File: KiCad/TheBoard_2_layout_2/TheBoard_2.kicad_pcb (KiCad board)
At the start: 2 copper layers, 150 x 100 mm, 165 parts, among them J1 Conn_01x03_Female, J2 Conn_01x03_Female, J3 Conn_01x16_Female, J4 DB37_Male_MountingHoles, J5 Conn_01x16_Female, J6 Conn_01x02_Male, J7 Conn_01x02_Pin, J8 Conn_01x02_Male, U1 MAX680CSA+T, U10 MCP6074-E/SL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

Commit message: power connection
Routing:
- net +2V5: track 300.7 -> 409.1 mm, vias 16 -> 17
- net +5V: track 412.5 -> 486.2 mm
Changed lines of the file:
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@@
   (segment (start 127.75 133.5) (end 136.75 133.5) (width 1.6) (layer "F.Cu") (net 1))
   (segment (start 146.75 121.75) (end 147 121.5) (width 1.6) (layer "F.Cu") (net 1))
+  (segment (start 144.75 141.5) (end 207.17 141.5) (width 1.6) (layer "F.Cu") (net 1))
+  (segment (start 136.75 133.5) (end 144.75 141.5) (width 1.6) (layer "F.Cu") (net 1))
   (via (at 108.30572 72.859279) (size 0.8) (drill 0.4) (layers "F.Cu" "B.Cu") (net 1))
   (via (at 200.5 103) (size 0.8) (drill 0.4) (layers "F.Cu" "B.Cu") (net 1))
@@
   (segment (start 108.30572 77.109279) (end 107.46822 77.109279) (width 0.6) (layer "F.Cu") (net 2))
   (segment (start 107.501779 118.366203) (end 108.201203 118.366203) (width 0.6) (layer "F.Cu") (net 2))
+  (segment (start 127.75 144.5) (end 208.75 144.5) (width 1.6) (layer "F.Cu") (net 2))
   (segment (start 200.5 98.5) (end 199.6625 98.5) (width 0.6) (layer "F.Cu") (net 2))
   (segment (start 199.6625 112.5) (end 200.5 112.5) (width 0.6) (layer "F.Cu") (net 2))
   (segment (start 108.4 99.775) (end 109.1925 99.775) (width 0.6) (layer "F.Cu") (net 2))
   (segment (start 108.375 113.75) (end 109.1675 113.75) (width 0.6) (layer "F.Cu") (net 2))
+  (segment (start 209.71 143.46) (end 209.71 141.5) (width 1.6) (layer "F.Cu") (net 2))
   (segment (start 200.5 76.75) (end 201.3375 76.75) (width 0.6) (layer "F.Cu") (net 2))
   (segment (start 108.201203 118.366203) (end 109.176779 118.366203) (width 0.6) (layer "F.Cu") (net 2))
@@
   (segment (start 199.524032 130.700961) (end 200.361532 130.700961) (width 0.6) (layer "F.Cu") (net 2))
   (segment (start 200.5 63) (end 201.3375 63) (width 0.6) (layer "F.Cu") (net 2))
+  (segment (start 209.75 143.5) (end 209.71 143.46) (width 1.6) (layer "F.Cu") (net 2))
+  (segment (start 208.75 144.5) (end 209.75 143.5) (width 1.6) (layer "F.Cu") (net 2))
   (segment (start 109.14322 63.109279) (end 108.30572 63.109279) (width 0.6) (layer "F.Cu") (net 2))
   (segment (start 199.6625 76.75) (end 200.5 76.75) (width 0.6) (layer "F.Cu") (net 2))
@@
   (segment (start 108.701203 132.616203) (end 109.426779 132.616203) (width 0.6) (layer "F.Cu") (net 2))
   (via (at 108.201203 118.366203) (size 0.8) (drill 0.4) (layers "F.Cu" "B.Cu") (net 2))
+  (via (at 127.75 144.5) (size 0.8) (drill 0.7) (layers "F.Cu" "B.Cu") (net 2))
   (via (at 108.701203 132.616203) (size 0.8) (drill 0.4) (layers "F.Cu" "B.Cu") (net 2))
   (via (at 200.5 63) (size 0.8) (drill 0.4) (layers "F.Cu" "B.Cu") (net 2))
@@
   (segment (start 200.466487 94.653994) (end 209.556006 94.653994) (width 1.6) (layer "B.Cu") (net 2))
   (segment (start 108.395 77.198559) (end 108.30572 77.109279) (width 1.6) (layer "B.Cu") (net 2))
+  (segment (start 120.585 144.5) (end 127.75 144.5) (width 1.6) (layer "B.Cu") (net 2))
   (segment (start 108.395 99.77) (end 108.4 99.775) (width 1.6) (layer "B.Cu") (net 2))
   (segment (start 99.21 53) (end 99.21 63.25) (width 1.6) (layer "B.Cu") (net 2))
@@
   (segment (start 108.375 118.192406) (end 108.201203 118.366203) (width 1.6) (layer "B.Cu") (net 2))
   (segment (start 209.71 112.5) (end 209.71 94.5) (width 1.6) (layer "B.Cu") (net 2))
+  (segment (start 108.701203 132.616203) (end 120.585 144.5) (width 1.6) (layer "B.Cu") (net 2))
   (segment (start 200.361532 130.700961) (end 209.660961 130.700961) (width 1.6) (layer "B.Cu") (net 2))
   (segment (start 102 132.5) (end 108.585 132.5) (width 1.6) (layer "B.Cu") (net 2))

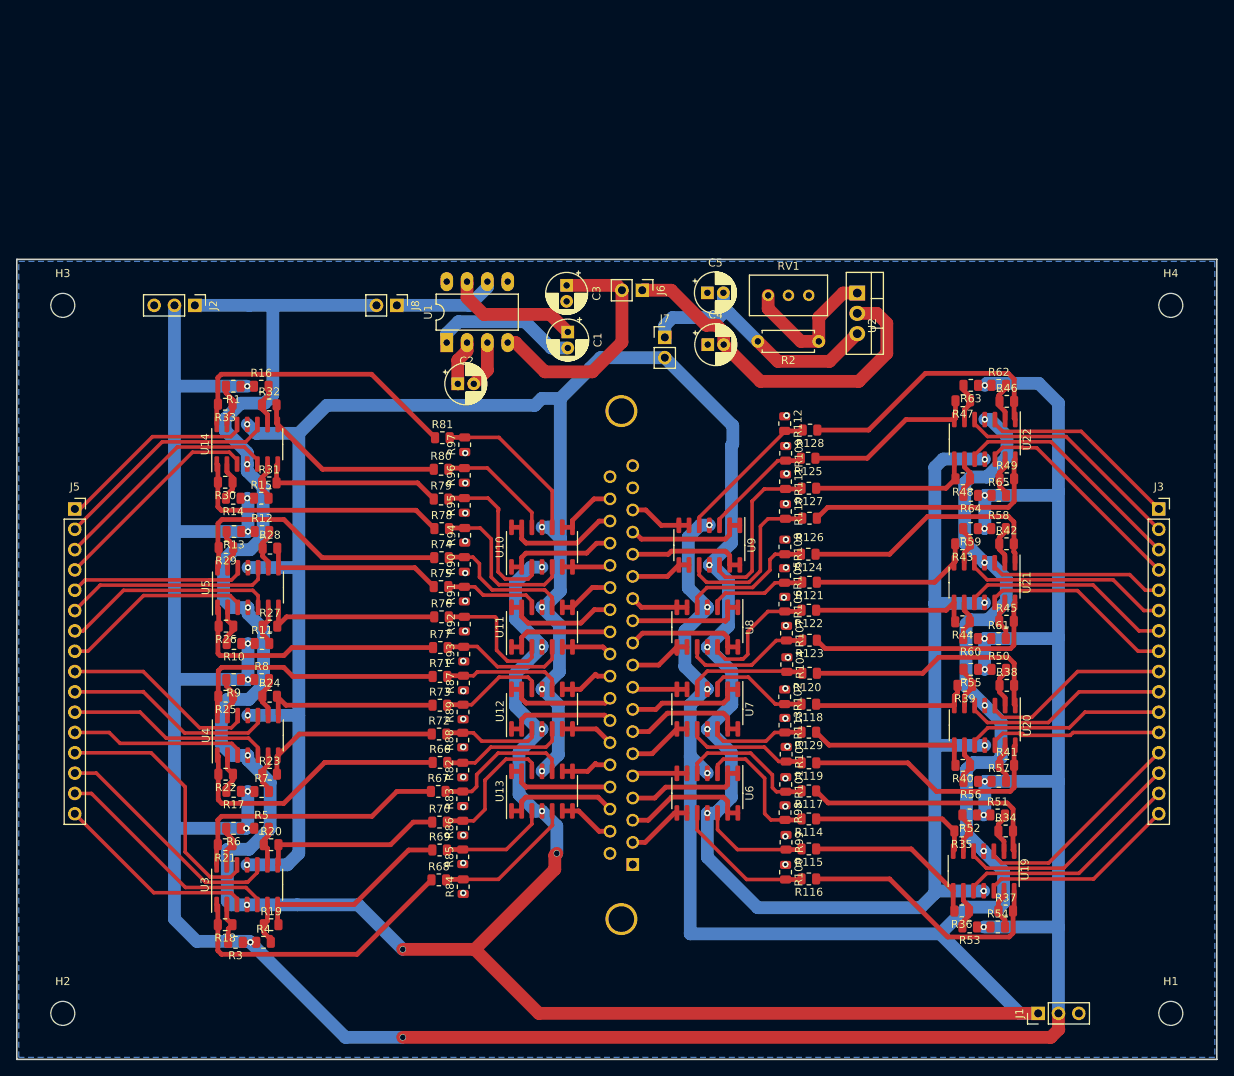
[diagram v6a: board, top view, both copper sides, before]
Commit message: Adding gnd to pot, cleaning vias and tracks
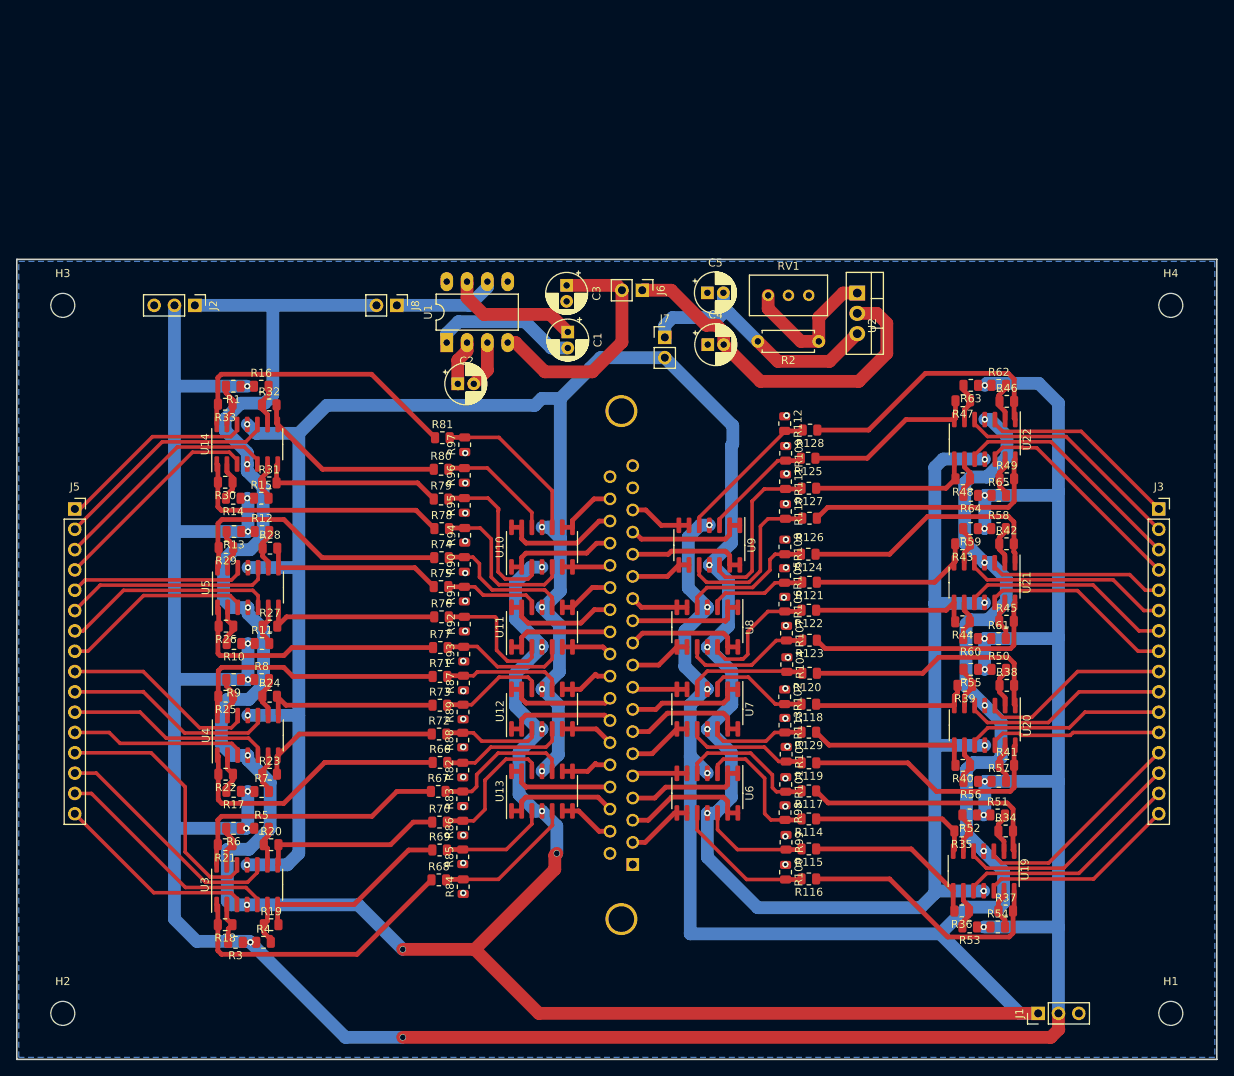
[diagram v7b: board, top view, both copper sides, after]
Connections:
- RV1 pad 1: unconnected-(RV1-Pad1) -> GND
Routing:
- net Net-(U8-VINC-): track 8.56 -> 7.73 mm
- net Net-(U8-VINA-): track 15.3 -> 14.7 mm
- net Net-(U9-VINB-): track 8.42 -> 7.83 mm
- net Net-(U12-VINB-): track 7.24 -> 6.67 mm
